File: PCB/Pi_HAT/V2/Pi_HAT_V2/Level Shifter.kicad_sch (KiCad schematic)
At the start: 9 parts, among them Q1 BSS138_RFG, Q2 BSS138_RFG, Q3 BSS138_RFG

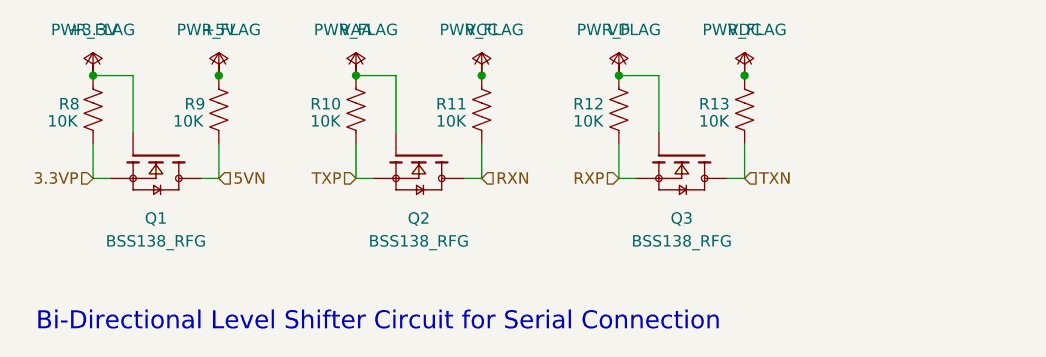
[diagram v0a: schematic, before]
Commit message: Finished Pi HAT V2
Double checked all 'new' PCB's and made gerbers for all along with a BOM.
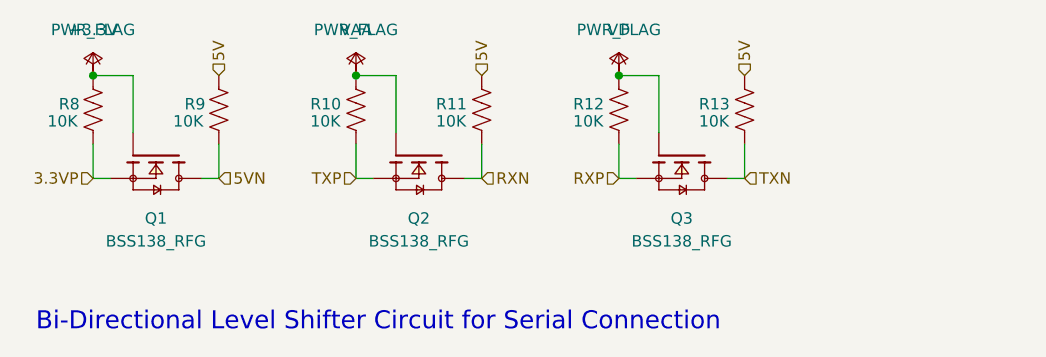
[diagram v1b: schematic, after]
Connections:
- net VCC is gone; now on net 5V: R11.1
- net VDC is gone; now on net 5V: R13.1
- net +5V renamed 5V
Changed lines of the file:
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@@
 (kicad_sch (version 20211123) (generator eeschema)
   (paper "A4")
-  (junction (at 119.38 92.075) (diameter 0) (color 0 0 0 0)
-  )
-  (junction (at 177.8 92.075) (diameter 0) (color 0 0 0 0)
-  )
   (junction (at 163.83 92.075) (diameter 0) (color 0 0 0 0)
-  )
-  (junction (at 148.59 92.075) (diameter 0) (color 0 0 0 0)
   )
   (junction (at 105.41 92.075) (diameter 0) (color 0 0 0 0)
@@
     (effects (font (size 1.27 1.27)) (justify left))
   )
+  (hierarchical_label "5V" (shape input) (at 177.8 92.075 90)
+    (effects (font (size 1.27 1.27)) (justify left))
+  )
   (hierarchical_label "RXP" (shape input) (at 163.83 103.505 180)
     (effects (font (size 1.27 1.27)) (justify right))
   )
+  (hierarchical_label "5V" (shape input) (at 119.38 92.075 90)
+    (effects (font (size 1.27 1.27)) (justify left))
+  )
   (hierarchical_label "TXP" (shape input) (at 134.62 103.505 180)
     (effects (font (size 1.27 1.27)) (justify right))
@@
     (effects (font (size 1.27 1.27)) (justify right))
   )
+  (hierarchical_label "5V" (shape input) (at 148.59 92.075 90)
+    (effects (font (size 1.27 1.27)) (justify left))
+  )
   (hierarchical_label "5VN" (shape input) (at 119.38 103.505 0)
     (effects (font (size 1.27 1.27)) (justify left))
@@
     (pin "1")
     (pin "2")
-  )
-  (symbol (lib_id "power:VDC") (at 177.8 92.075 0) (unit 1)
-    (in_bom yes) (on_board yes)
-    (property "Reference" "#PWR0122" (id 0) (at 177.8 94.615 0)
-      (effects (font (size 1.27 1.27)) hide)
-    )
-    (property "Value" "VDC" (id 1) (at 177.8 86.995 0))
-    (property "Footprint" "" (id 2) (at 177.8 92.075 0)
-      (effects (font (size 1.27 1.27)) hide)
-    )
-    (property "Datasheet" "" (id 3) (at 177.8 92.075 0)
-      (effects (font (size 1.27 1.27)) hide)
-    )
-    (pin "1")
   )
   (symbol (lib_id "power:VD") (at 163.83 92.075 0) (unit 1)
@@
     (pin "3")
   )
-  (symbol (lib_id "power:VCC") (at 148.59 92.075 0) (unit 1)
-    (in_bom yes) (on_board yes)
-    (property "Reference" "#PWR0121" (id 0) (at 148.59 95.885 0)
-      (effects (font (size 1.27 1.27)) hide)
-    )
-    (property "Value" "VCC" (id 1) (at 148.59 86.995 0))
-    (property "Footprint" "" (id 2) (at 148.59 92.075 0)
-      (effects (font (size 1.27 1.27)) hide)
-    )
-    (property "Datasheet" "" (id 3) (at 148.59 92.075 0)
-      (effects (font (size 1.27 1.27)) hide)
-    )
-    (pin "1")
-  )
   (symbol (lib_id "Device:R_US") (at 148.59 95.885 0) (unit 1)
     (in_bom yes) (on_board yes)
@@
     (pin "3")
   )
-  (symbol (lib_id "power:PWR_FLAG") (at 177.8 92.075 0) (unit 1)
-    (in_bom yes) (on_board yes) (fields_autoplaced)
-    (property "Reference" "#FLG0108" (id 0) (at 177.8 90.17 0)
-      (effects (font (size 1.27 1.27)) hide)
-    )
-    (property "Value" "PWR_FLAG" (id 1) (at 177.8 86.995 0))
-    (property "Footprint" "" (id 2) (at 177.8 92.075 0)
-      (effects (font (size 1.27 1.27)) hide)
-    )
-    (property "Datasheet" "~" (id 3) (at 177.8 92.075 0)
-      (effects (font (size 1.27 1.27)) hide)
-    )
-    (pin "1")
-  )
   (symbol (lib_id "power:PWR_FLAG") (at 163.83 92.075 0) (unit 1)
     (in_bom yes) (on_board yes) (fields_autoplaced)
@@
       (effects (font (size 1.27 1.27)) hide)
     )
-    (pin "1")
-  )
-  (symbol (lib_id "power:PWR_FLAG") (at 119.38 92.075 0) (unit 1)
-    (in_bom yes) (on_board yes) (fields_autoplaced)
-    (property "Reference" "#FLG0104" (id 0) (at 119.38 90.17 0)
-      (effects (font (size 1.27 1.27)) hide)
-    )
-    (property "Value" "PWR_FLAG" (id 1) (at 119.38 86.995 0))
-    (property "Footprint" "" (id 2) (at 119.38 92.075 0)
-      (effects (font (size 1.27 1.27)) hide)
-    )
-    (property "Datasheet" "~" (id 3) (at 119.38 92.075 0)
-      (effects (font (size 1.27 1.27)) hide)
-    )
-    (pin "1")
-  )
-  (symbol (lib_id "power:+5V") (at 119.38 92.075 0) (unit 1)
-    (in_bom yes) (on_board yes)
-    (property "Reference" "#PWR0118" (id 0) (at 119.38 95.885 0)
-      (effects (font (size 1.27 1.27)) hide)
-    )
-    (property "Value" "+5V" (id 1) (at 119.38 86.995 0))
-    (property "Footprint" "" (id 2) (at 119.38 92.075 0)
-      (effects (font (size 1.27 1.27)) hide)
-    )
-    (property "Datasheet" "" (id 3) (at 119.38 92.075 0)
-      (effects (font (size 1.27 1.27)) hide)
-    )
-    (pin "1")
-  )
-  (symbol (lib_id "power:PWR_FLAG") (at 148.59 92.075 0) (unit 1)
-    (in_bom yes) (on_board yes) (fields_autoplaced)
-    (property "Reference" "#FLG0107" (id 0) (at 148.59 90.17 0)
-      (effects (font (size 1.27 1.27)) hide)
-    )
-    (property "Value" "PWR_FLAG" (id 1) (at 148.59 86.995 0))
-    (property "Footprint" "" (id 2) (at 148.59 92.075 0)
-      (effects (font (size 1.27 1.27)) hide)
-    )
-    (property "Datasheet" "~" (id 3) (at 148.59 92.075 0)
-      (effects (font (size 1.27 1.27)) hide)
-    )
